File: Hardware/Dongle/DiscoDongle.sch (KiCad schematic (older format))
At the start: 22 parts, among them J1 RJ45, P1 USB_B, P2 FTDI, U1 FT232RL, U2 ISL81487E

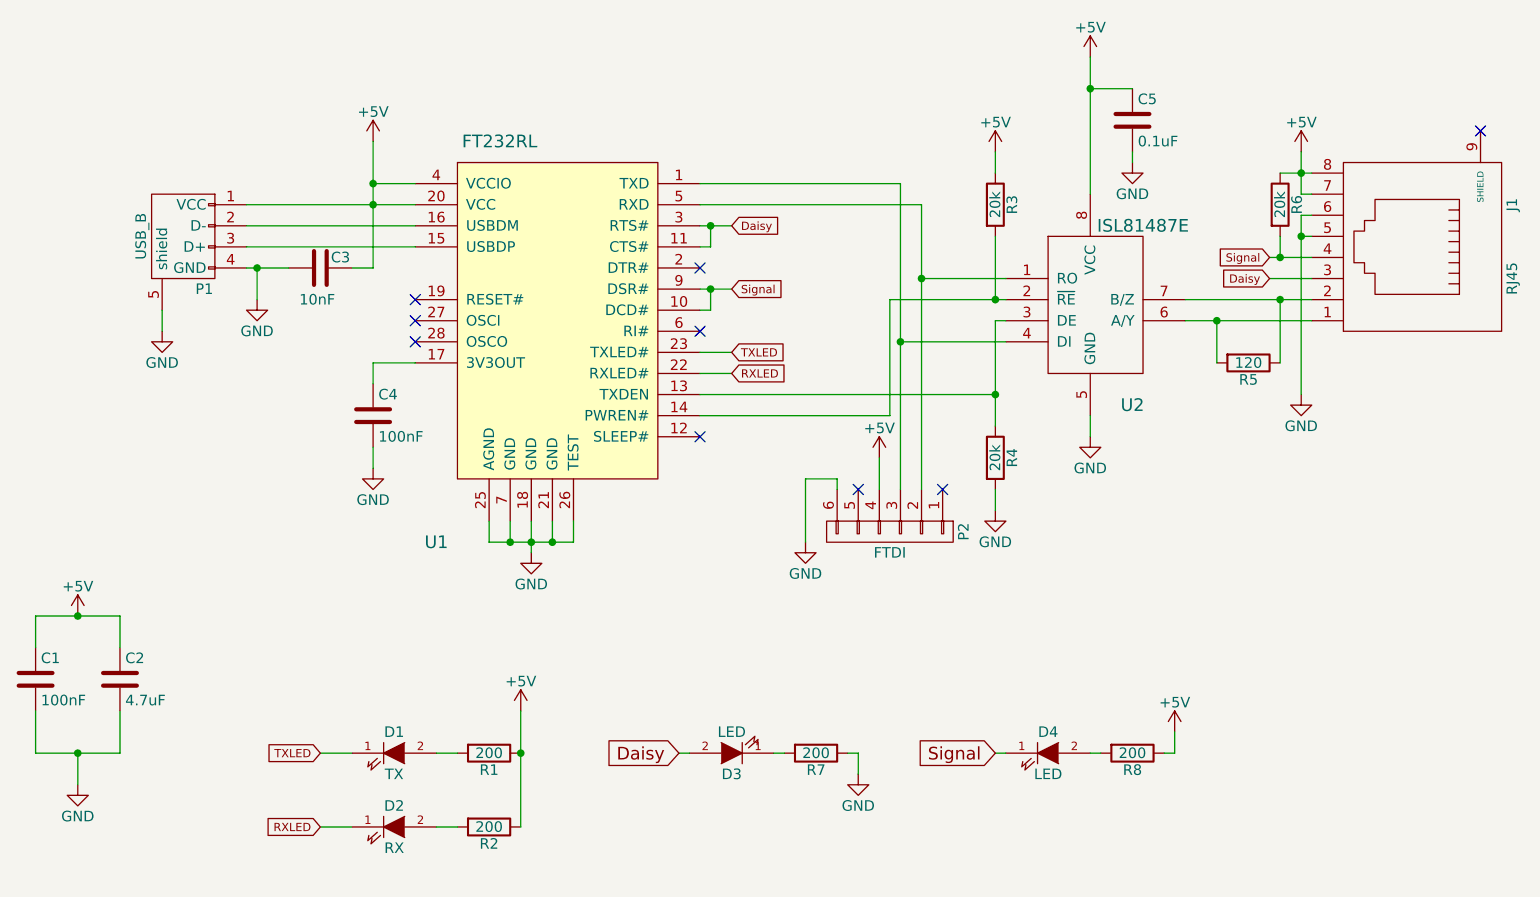
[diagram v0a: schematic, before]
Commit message: Update the DiscoDongle with more LEDs and pull-up on daisy line.
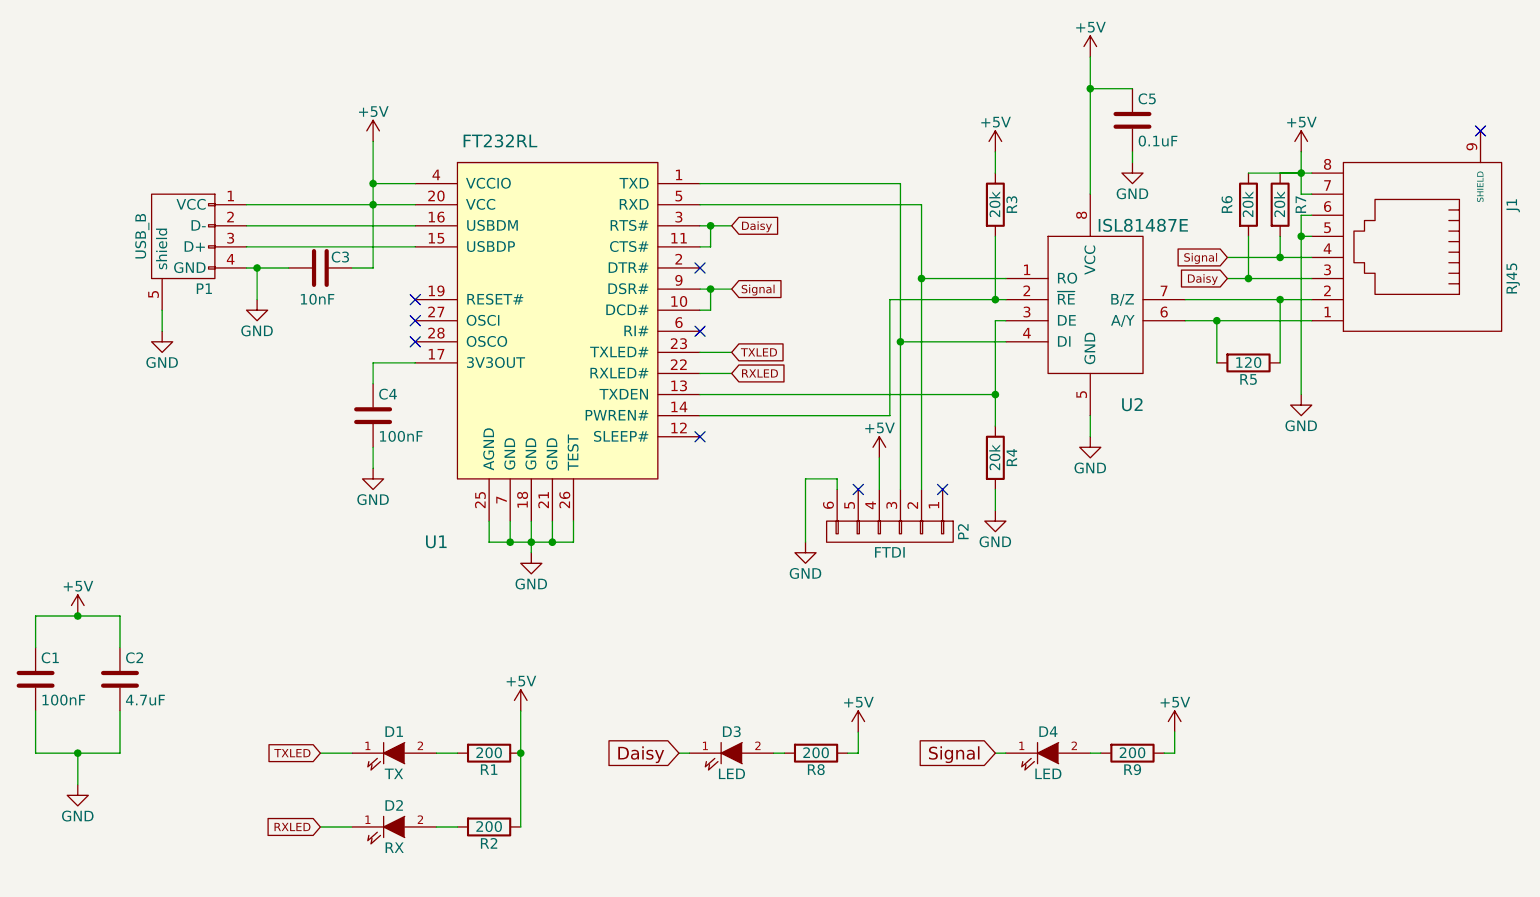
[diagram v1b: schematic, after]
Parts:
- added R6: 20k, Resistors_SMD:R_0805, symbol R
- renumbered R6 to R7, R7 to R8, R8 to R9
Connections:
- net +5V: now also R8.1, R6.1
- net Daisy: now also D3.1 (K), R6.2; no longer D3.2 (A)
- net GND: no longer R8.1
- net at R8.2: now also D3.2 (A); no longer D3.1 (K)
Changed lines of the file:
@@
 Text GLabel 4500 2150 2    39   Input ~ 0
 Signal
-Text GLabel 7050 2100 0    39   Input ~ 0
+Text GLabel 6850 2100 0    39   Input ~ 0
 Daisy
-Text GLabel 7050 2000 0    39   Input ~ 0
+Text GLabel 6850 2000 0    39   Input ~ 0
 Signal
 $Comp
@@
 NoConn ~ 5100 3100
 $Comp
-L R R6
+L R R7
 U 1 1 5747F3E8
 P 7100 1750
-F 0 "R6" V 7180 1750 50  0000 C CNN
+F 0 "R7" V 7200 1750 50  0000 C CNN
 F 1 "20k" V 7100 1750 50  0000 C CNN
 F 2 "Resistors_SMD:R_0805" V 7030 1750 50  0001 C CNN
@@
 F 3 "" H 4500 4350 50  0000 C CNN
 	1    4500 4350
-	-1   0    0    1
-$EndComp
-$Comp
-L R R7
+	1    0    0    -1
+$EndComp
+$Comp
+L R R8
 U 1 1 5748F6BB
 P 4900 4350
-F 0 "R7" V 4980 4350 50  0000 C CNN
+F 0 "R8" V 4980 4350 50  0000 C CNN
 F 1 "200" V 4900 4350 50  0000 C CNN
 F 2 "Resistors_SMD:R_0805" V 4830 4350 50  0001 C CNN
@@
 	1    4900 4350
 	0    1    1    0
-$EndComp
-$Comp
-L GND #PWR08
-U 1 1 5748FB0F
-P 5100 4450
-F 0 "#PWR08" H 5100 4200 50  0001 C CNN
-F 1 "GND" H 5100 4300 50  0000 C CNN
-F 2 "" H 5100 4450 50  0000 C CNN
-F 3 "" H 5100 4450 50  0000 C CNN
-	1    5100 4450
-	1    0    0    -1
 $EndComp
 $Comp
@@
 $EndComp
 $Comp
-L R R8
+L R R9
 U 1 1 57490EAE
 P 6400 4350
-F 0 "R8" V 6480 4350 50  0000 C CNN
+F 0 "R9" V 6480 4350 50  0000 C CNN
 F 1 "200" V 6400 4350 50  0000 C CNN
 F 2 "Resistors_SMD:R_0805" V 6330 4350 50  0001 C CNN
@@
 $EndComp
 NoConn ~ 4350 2050
+$Comp
+L R R6
+U 1 1 5765F021
+P 6950 1750
+F 0 "R6" V 6850 1750 50  0000 C CNN
+F 1 "20k" V 6950 1750 50  0000 C CNN
+F 2 "Resistors_SMD:R_0805" V 6880 1750 50  0001 C CNN
+F 3 "" H 6950 1750 50  0000 C CNN
+	1    6950 1750
+	1    0    0    -1
+$EndComp
 Wire Wire Line
 	1800 2250 1800 2350
@@
 	2550 4350 2700 4350
 Wire Wire Line
-	4350 1850 4500 1850
-Connection ~ 4400 1850
-Wire Wire Line
 	4350 2250 4400 2250
 Wire Wire Line
@@
 Connection ~ 4400 2150
 Wire Wire Line
-	7050 2000 7250 2000
+	6850 2000 7250 2000
 Wire Wire Line
 	5750 1900 5750 2200
@@
 Connection ~ 1400 4350
 Wire Wire Line
-	7050 2100 7250 2100
+	6850 2100 7250 2100
 Wire Wire Line
 	5750 3200 5750 3100
@@
 	4700 4350 4750 4350
 Wire Wire Line
-	5050 4350 5100 4350
-Wire Wire Line
-	5100 4350 5100 4450
-Wire Wire Line
 	6550 4350 6600 4350
 Wire Wire Line
@@
 Wire Wire Line
 	6200 2750 6200 2850
-Wire Wire Line
-	4350 1950 4400 1950
-Wire Wire Line
-	4400 1950 4400 1850
 Wire Wire Line
 	3350 3250 3350 3350
@@
 	2250 2050 2250 2200
 Connection ~ 2250 2050
+Wire Wire Line
+	6950 1900 6950 2100
+Connection ~ 6950 2100
+Wire Wire Line
+	6950 1600 7200 1600
+Connection ~ 4400 1850
+Wire Wire Line
+	4350 1850 4500 1850
+Wire Wire Line
+	4400 1950 4400 1850
+Wire Wire Line
+	4350 1950 4400 1950
+$Comp
+L +5V #PWR?
+U 1 1 576751A3
+P 5100 4250
+F 0 "#PWR?" H 5100 4100 50  0001 C CNN
+F 1 "+5V" H 5100 4390 50  0000 C CNN
+F 2 "" H 5100 4250 50  0000 C CNN
+F 3 "" H 5100 4250 50  0000 C CNN
+	1    5100 4250
+	1    0    0    -1
+$EndComp
+Wire Wire Line
+	5100 4250 5100 4350
+Wire Wire Line
+	5100 4350 5050 4350
 $EndSCHEMATC

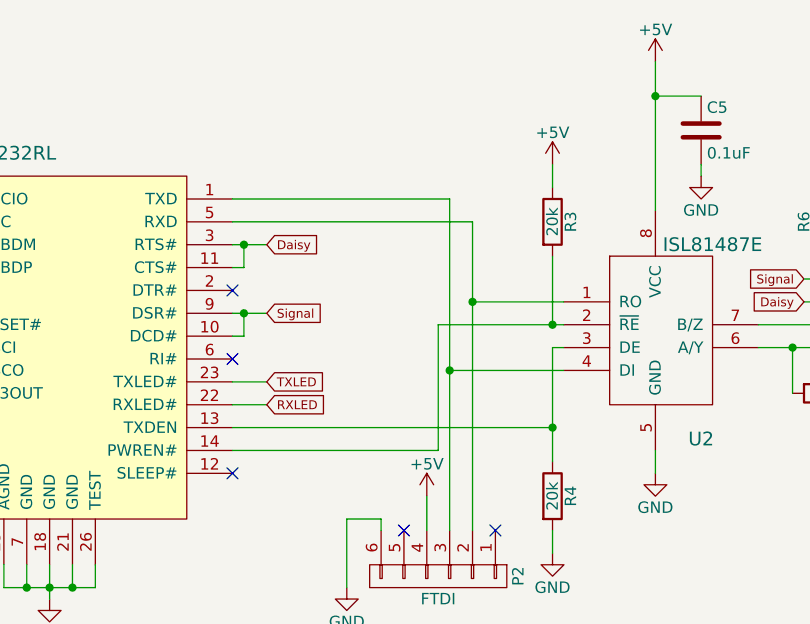
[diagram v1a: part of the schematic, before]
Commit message: Tie the RE and DE together on the TXEN line of FTDI
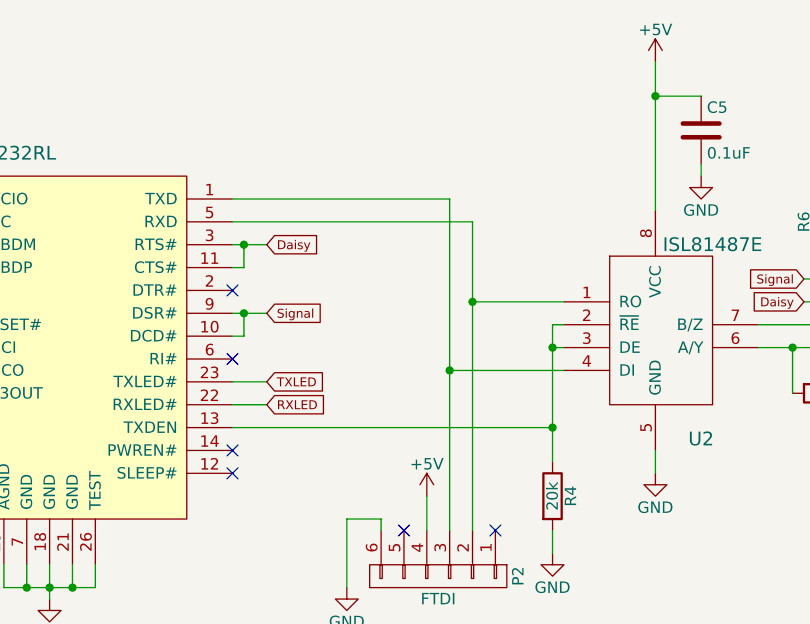
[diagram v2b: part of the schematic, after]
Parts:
- removed R3: 20k, Resistors_SMD:R_0805, symbol R
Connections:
- net at R4.1, U1.13 (TXDEN), U2.3 (DE): now also U2.2 (~RE)
- net at U1.14 (PWREN#): no longer U2.2 (~RE)
- no-connect marks 9 -> 10
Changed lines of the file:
@@
 Signal
-$Comp
-L R R3
-U 1 1 5746C653
-P 5750 1750
-F 0 "R3" V 5830 1750 50  0000 C CNN
-F 1 "20k" V 5750 1750 50  0000 C CNN
-F 2 "Resistors_SMD:R_0805" V 5680 1750 50  0001 C CNN
-F 3 "" H 5750 1750 50  0000 C CNN
-	1    5750 1750
-	1    0    0    -1
-$EndComp
-$Comp
-L +5V #PWR06
-U 1 1 5746C6F5
-P 5750 1500
-F 0 "#PWR06" H 5750 1350 50  0001 C CNN
-F 1 "+5V" H 5750 1640 50  0000 C CNN
-F 2 "" H 5750 1500 50  0000 C CNN
-F 3 "" H 5750 1500 50  0000 C CNN
-	1    5750 1500
-	1    0    0    -1
-$EndComp
 $Comp
 L C C5
@@
 	2800 2900 2800 3000
 Wire Wire Line
-	4350 2750 5250 2750
-Wire Wire Line
-	5250 2750 5250 2200
-Wire Wire Line
-	5250 2200 5800 2200
-Wire Wire Line
 	4350 2650 5750 2650
 Wire Wire Line
-	5750 2300 5750 2800
+	5750 2200 5750 2800
 Wire Wire Line
 	5750 2300 5800 2300
@@
 Wire Wire Line
 	6850 2000 7250 2000
-Wire Wire Line
-	5750 1900 5750 2200
-Connection ~ 5750 2200
-Wire Wire Line
-	5750 1500 5750 1600
 Wire Wire Line
 	6400 1200 6200 1200
@@
 Wire Wire Line
 	5100 4350 5050 4350
+Wire Wire Line
+	5800 2200 5750 2200
+Connection ~ 5750 2300
+NoConn ~ 4350 2750
 $EndSCHEMATC
